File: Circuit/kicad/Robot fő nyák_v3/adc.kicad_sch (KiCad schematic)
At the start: 9 parts, among them U28 ADC1283, U29 ADC1283, U30 ADC1283, U31 ADS1115IDGS, U32 ADS1115IDGS, U33 ADS1115IDGS

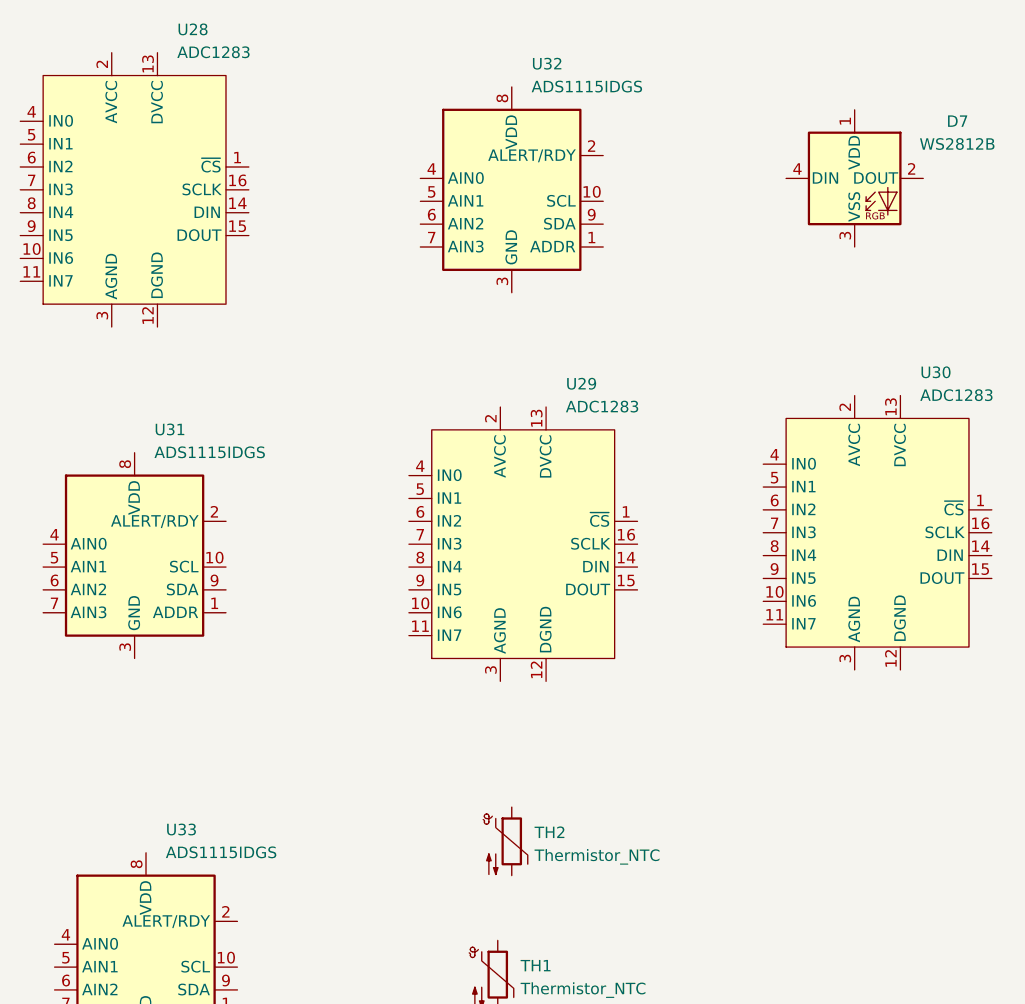
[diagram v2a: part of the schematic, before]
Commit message: kicad v0.1 footprint- assing spi finish
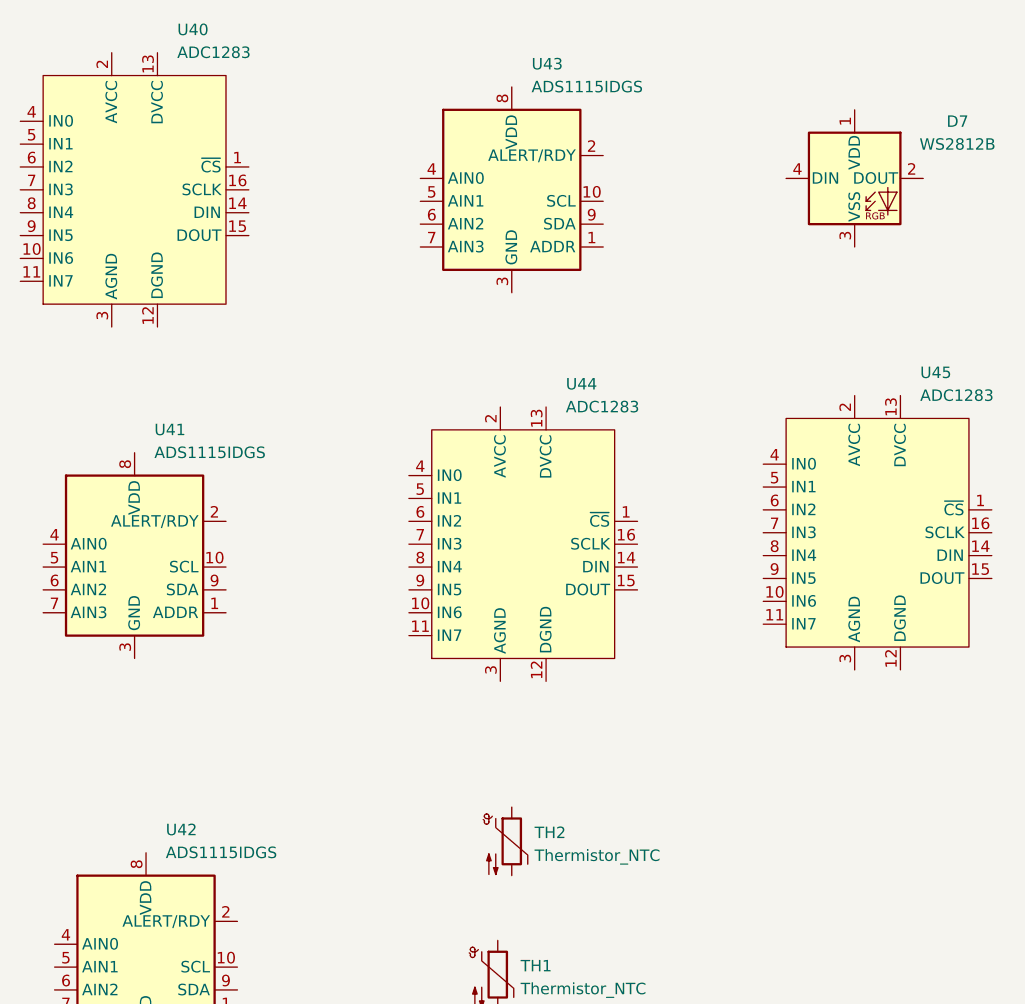
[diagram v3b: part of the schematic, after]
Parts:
- TH1, TH2: footprint (none) -> Resistor_THT:R_Axial_DIN0204_L3.6mm_D1.6mm_P5.08mm_Horizontal
- renumbered U28 to U40, U31 to U41, U33 to U42, U32 to U43, U29 to U44, U30 to U45
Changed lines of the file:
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@@
 		(dnp no)
 		(fields_autoplaced yes)
-		(property "Reference" "U33"
+		(property "Reference" "U42"
 			(at 42.8341 111.76 0)
 			(effects
@@
 			(project "CM5IO"
 				(path "/e63e39d7-6ac0-4ffd-8aa3-1841a4541b55/a83afe30-5c7e-43cb-a5b2-f6f97a0812b3/ea85c6ab-21e3-4ada-9ce7-e96fd4df8568"
-					(reference "U33")
+					(reference "U42")
 					(unit 1)
 				)
@@
 		(dnp no)
 		(fields_autoplaced yes)
-		(property "Reference" "U28"
+		(property "Reference" "U40"
 			(at 44.1041 22.86 0)
 			(effects
@@
 			(project "CM5IO"
 				(path "/e63e39d7-6ac0-4ffd-8aa3-1841a4541b55/a83afe30-5c7e-43cb-a5b2-f6f97a0812b3/ea85c6ab-21e3-4ada-9ce7-e96fd4df8568"
-					(reference "U28")
+					(reference "U40")
 					(unit 1)
 				)
@@
 		(dnp no)
 		(fields_autoplaced yes)
-		(property "Reference" "U31"
+		(property "Reference" "U41"
 			(at 41.5641 67.31 0)
 			(effects
@@
 			(project "CM5IO"
 				(path "/e63e39d7-6ac0-4ffd-8aa3-1841a4541b55/a83afe30-5c7e-43cb-a5b2-f6f97a0812b3/ea85c6ab-21e3-4ada-9ce7-e96fd4df8568"
-					(reference "U31")
+					(reference "U41")
 					(unit 1)
 				)
@@
 		(dnp no)
 		(fields_autoplaced yes)
-		(property "Reference" "U29"
+		(property "Reference" "U44"
 			(at 87.2841 62.23 0)
 			(effects
@@
 			(project "CM5IO"
 				(path "/e63e39d7-6ac0-4ffd-8aa3-1841a4541b55/a83afe30-5c7e-43cb-a5b2-f6f97a0812b3/ea85c6ab-21e3-4ada-9ce7-e96fd4df8568"
-					(reference "U29")
+					(reference "U44")
 					(unit 1)
 				)
@@
 		(dnp no)
 		(fields_autoplaced yes)
-		(property "Reference" "U32"
+		(property "Reference" "U43"
 			(at 83.4741 26.67 0)
 			(effects
@@
 			(project "CM5IO"
 				(path "/e63e39d7-6ac0-4ffd-8aa3-1841a4541b55/a83afe30-5c7e-43cb-a5b2-f6f97a0812b3/ea85c6ab-21e3-4ada-9ce7-e96fd4df8568"
-					(reference "U32")
+					(reference "U43")
 					(unit 1)
 				)
@@
 			)
 		)
-		(property "Footprint" ""
+		(property "Footprint" "Resistor_THT:R_Axial_DIN0204_L3.6mm_D1.6mm_P5.08mm_Horizontal"
 			(at 81.28 111.76 0)
 			(effects
@@
 			)
 		)
-		(property "Footprint" ""
+		(property "Footprint" "Resistor_THT:R_Axial_DIN0204_L3.6mm_D1.6mm_P5.08mm_Horizontal"
 			(at 79.7228 126.5689 0)
 			(effects
@@
 		(dnp no)
 		(fields_autoplaced yes)
-		(property "Reference" "U30"
+		(property "Reference" "U45"
 			(at 126.6541 60.96 0)
 			(effects
@@
 			(project "CM5IO"
 				(path "/e63e39d7-6ac0-4ffd-8aa3-1841a4541b55/a83afe30-5c7e-43cb-a5b2-f6f97a0812b3/ea85c6ab-21e3-4ada-9ce7-e96fd4df8568"
-					(reference "U30")
-					(unit 1)
-				)
+					(reference "U45")
+					(unit 1)
+				)

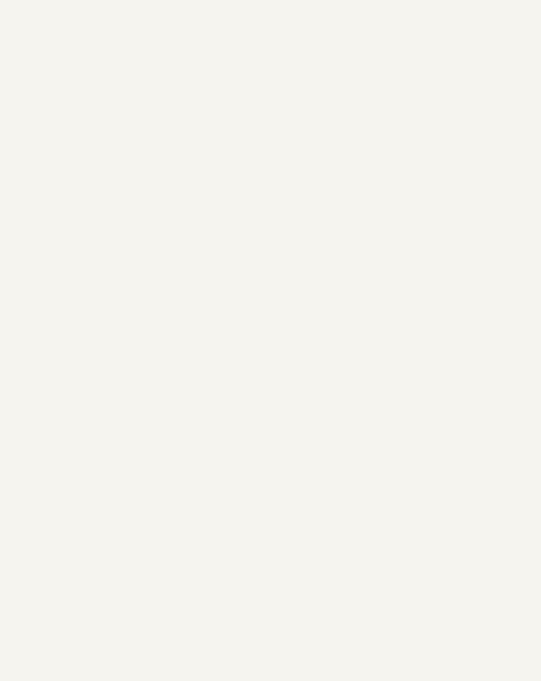
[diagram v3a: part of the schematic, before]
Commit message: kicad  i2c and spi mux fixed and bugfixs
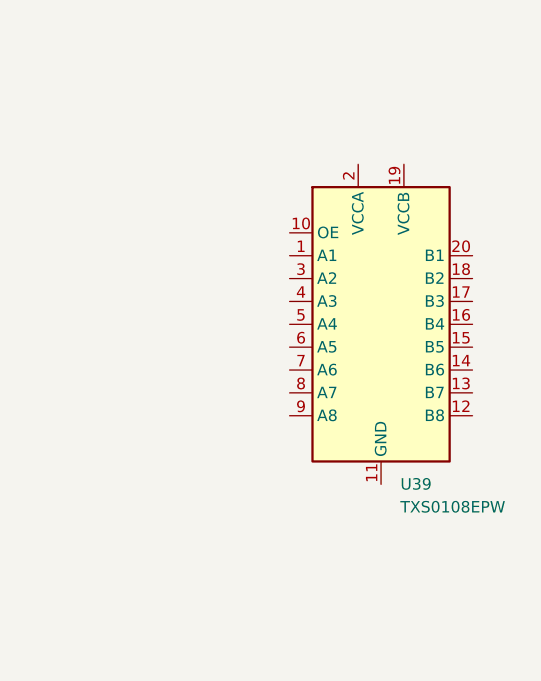
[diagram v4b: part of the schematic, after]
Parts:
- added U39: TXS0108EPW, Package_SO:TSSOP-20_4.4x6.5mm_P0.65mm, symbol Logic_LevelTranslator:TXS0108EPW
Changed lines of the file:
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@@
 	(paper "A4")
+	(symbol
+		(lib_id "Logic_LevelTranslator:TXS0108EPW")
+		(at 190.5 76.2 0)
+		(unit 1)
+		(exclude_from_sim no)
+		(in_bom yes)
+		(on_board yes)
+		(dnp no)
+		(fields_autoplaced yes)
+		(property "Reference" "U39"
+			(at 192.6433 93.98 0)
+			(effects
+				(font
+					(size 1.27 1.27)
+				)
+				(justify left)
+			)
+		)
+		(property "Value" "TXS0108EPW"
+			(at 192.6433 96.52 0)
+			(effects
+				(font
+					(size 1.27 1.27)
+				)
+				(justify left)
+			)
+		)
+		(property "Footprint" "Package_SO:TSSOP-20_4.4x6.5mm_P0.65mm"
+			(at 190.5 95.25 0)
+			(effects
+				(font
+					(size 1.27 1.27)
+				)
+				(hide yes)
+			)
+		)
+		(property "Datasheet" "www.ti.com/lit/ds/symlink/txs0108e.pdf"
+			(at 190.5 78.74 0)
+			(effects
+				(font
+					(size 1.27 1.27)
+				)
+				(hide yes)
+			)
+		)
+		(property "Description" "Bidirectional  level-shifting voltage translator, TSSOP-20"
+			(at 190.5 76.2 0)
+			(effects
+				(font
+					(size 1.27 1.27)
+				)
+				(hide yes)
+			)
+		)
+		(pin "3"
+		)
+		(pin "10"
+		)
+		(pin "1"
+		)
+		(pin "4"
+		)
+		(pin "6"
+		)
+		(pin "7"
+		)
+		(pin "5"
+		)
+		(pin "8"
+		)
+		(pin "11"
+		)
+		(pin "16"
+		)
+		(pin "18"
+		)
+		(pin "17"
+		)
+		(pin "20"
+		)
+		(pin "14"
+		)
+		(pin "13"
+		)
+		(pin "9"
+		)
+		(pin "2"
+		)
+		(pin "19"
+		)
+		(pin "15"
+		)
+		(pin "12"
+		)
+		(instances
+			(project "CM5IO"
+				(path "/e63e39d7-6ac0-4ffd-8aa3-1841a4541b55/a83afe30-5c7e-43cb-a5b2-f6f97a0812b3/ea85c6ab-21e3-4ada-9ce7-e96fd4df8568"
+					(reference "U39")
+					(unit 1)
+				)
+			)
+		)
+	)
 	(symbol
 		(lib_id "Analog_ADC:ADS1115IDGS")

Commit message: readme updated kicad circuit V1
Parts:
- renumbered U40 to U38, U41 to U39, U42 to U40, U43 to U41, U44 to U42, U45 to U43, U39 to U44
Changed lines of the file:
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@@
 		(dnp no)
 		(fields_autoplaced yes)
-		(property "Reference" "U39"
+		(property "Reference" "U44"
 			(at 192.6433 93.98 0)
 			(effects
@@
 			(project "CM5IO"
 				(path "/e63e39d7-6ac0-4ffd-8aa3-1841a4541b55/a83afe30-5c7e-43cb-a5b2-f6f97a0812b3/ea85c6ab-21e3-4ada-9ce7-e96fd4df8568"
-					(reference "U39")
+					(reference "U44")
 					(unit 1)
 				)
@@
 		(dnp no)
 		(fields_autoplaced yes)
-		(property "Reference" "U42"
+		(property "Reference" "U40"
 			(at 42.8341 111.76 0)
 			(effects
@@
 			(project "CM5IO"
 				(path "/e63e39d7-6ac0-4ffd-8aa3-1841a4541b55/a83afe30-5c7e-43cb-a5b2-f6f97a0812b3/ea85c6ab-21e3-4ada-9ce7-e96fd4df8568"
-					(reference "U42")
+					(reference "U40")
 					(unit 1)
 				)
@@
 		(dnp no)
 		(fields_autoplaced yes)
-		(property "Reference" "U40"
+		(property "Reference" "U38"
 			(at 44.1041 22.86 0)
 			(effects
@@
 			(project "CM5IO"
 				(path "/e63e39d7-6ac0-4ffd-8aa3-1841a4541b55/a83afe30-5c7e-43cb-a5b2-f6f97a0812b3/ea85c6ab-21e3-4ada-9ce7-e96fd4df8568"
-					(reference "U40")
+					(reference "U38")
 					(unit 1)
 				)
@@
 		(dnp no)
 		(fields_autoplaced yes)
-		(property "Reference" "U41"
+		(property "Reference" "U39"
 			(at 41.5641 67.31 0)
 			(effects
@@
 			(project "CM5IO"
 				(path "/e63e39d7-6ac0-4ffd-8aa3-1841a4541b55/a83afe30-5c7e-43cb-a5b2-f6f97a0812b3/ea85c6ab-21e3-4ada-9ce7-e96fd4df8568"
-					(reference "U41")
+					(reference "U39")
 					(unit 1)
 				)
@@
 		(dnp no)
 		(fields_autoplaced yes)
-		(property "Reference" "U44"
+		(property "Reference" "U42"
 			(at 87.2841 62.23 0)
 			(effects
@@
 			(project "CM5IO"
 				(path "/e63e39d7-6ac0-4ffd-8aa3-1841a4541b55/a83afe30-5c7e-43cb-a5b2-f6f97a0812b3/ea85c6ab-21e3-4ada-9ce7-e96fd4df8568"
-					(reference "U44")
+					(reference "U42")
 					(unit 1)
 				)
@@
 		(dnp no)
 		(fields_autoplaced yes)
-		(property "Reference" "U43"
+		(property "Reference" "U41"
 			(at 83.4741 26.67 0)
 			(effects
@@
 			(project "CM5IO"
 				(path "/e63e39d7-6ac0-4ffd-8aa3-1841a4541b55/a83afe30-5c7e-43cb-a5b2-f6f97a0812b3/ea85c6ab-21e3-4ada-9ce7-e96fd4df8568"
-					(reference "U43")
+					(reference "U41")
 					(unit 1)
 				)
@@
 		(dnp no)
 		(fields_autoplaced yes)
-		(property "Reference" "U45"
+		(property "Reference" "U43"
 			(at 126.6541 60.96 0)
 			(effects
@@
 			(project "CM5IO"
 				(path "/e63e39d7-6ac0-4ffd-8aa3-1841a4541b55/a83afe30-5c7e-43cb-a5b2-f6f97a0812b3/ea85c6ab-21e3-4ada-9ce7-e96fd4df8568"
-					(reference "U45")
-					(unit 1)
-				)
+					(reference "U43")
+					(unit 1)
+				)
